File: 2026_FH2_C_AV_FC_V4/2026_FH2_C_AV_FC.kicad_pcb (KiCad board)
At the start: 4 copper layers, 80 x 80 mm, 258 parts, among them IC1 BMP390, IC2 BMP390, IC3 BMP390, IC4 BMP390, IC5 TPS22919DCKR, IC6 TPS22919DCKR, IC7 TPS22919DCKR, IC8 ADXL375BCCZ, IC9 CD4051BPWR, J1 CON-SMA-EDGE-S, J10 MUSB-05-S-B-SM-A-K-TR, J11 DIN41612_02x16_AB, J2 Screw_Terminal_01x02, J3 Screw_Terminal_01x02, J4 Screw_Terminal_01x02, J5 Screw_Terminal_01x02, J6 Micro_SD_Card_Det_Hirose_DM3AT, J7 Conn_01x04_Pin, J8 Conn_01x04_Pin, J9 MUSB-05-S-B-SM-A-K-TR, Q1 IRLML2502, Q2 IRLML6344TRPBF, Q3 IRLML6344TRPBF, Q4 IRLML6344TRPBF, Q5 IRLML6344TRPBF, Q6 IRLML6344TRPBF, Q7 IRLML6344TRPBF, SW1 SW_SPDT, SW2 SW_Push_SPDT, U1 MCP1727-3302xSN, U10 ICM-45605, U11 ICM-45605, U12 MAX3226, U13 SPINE_LT3960, U14 MCP2542FDxMF, U15 MCP2542FDxMF, U16 TMP1075DSG, U2 TPS2116DRL, U3 STM32H743ZITx, U4 RGBLED_1, U5 RGBLED_2, U6 RGBLED_3, U7 MAX-M10S, U8 ICM-45605, U9 ICM-45605, Y1 26Mhz

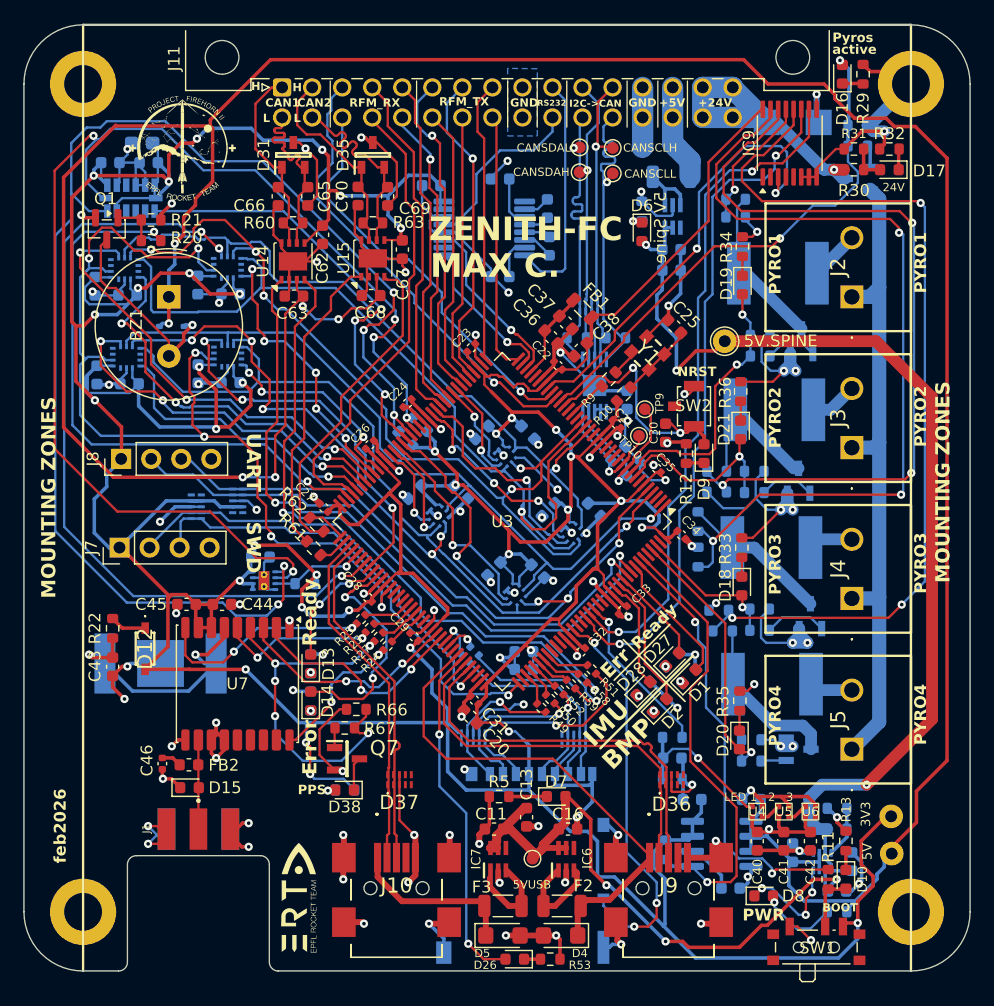
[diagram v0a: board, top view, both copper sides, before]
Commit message: FC FIX: DIN41612 was not centered
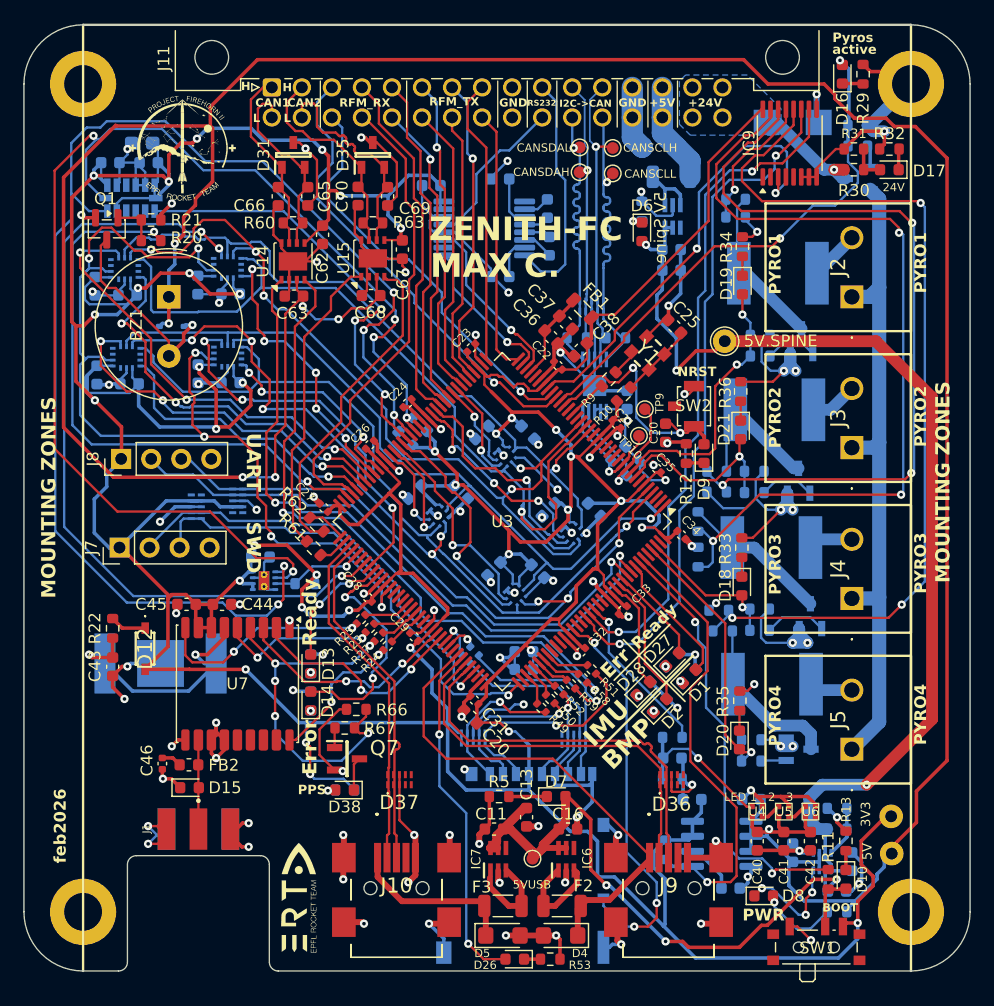
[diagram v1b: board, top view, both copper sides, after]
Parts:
- moved J11 0.87 mm to (140.0, 51.3)
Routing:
- net +24V: track 24.3 -> 9.47 mm
- net /Project Architecture/CAN RS232 and other connections/TX_RS232: track 15.0 -> 13.5 mm
- net /Project Architecture/CAN RS232 and other connections/CAN2_L: track 17.6 -> 18.9 mm
- net /Project Architecture/CAN RS232 and other connections/CANSCLL: track 27.1 -> 26.0 mm
- net /Project Architecture/SPINE/SPI_RFM_TX_MOSI: track 28.0 -> 27.0 mm
- net /Project Architecture/CAN RS232 and other connections/CAN2_H: track 17.6 -> 18.3 mm
- net /Project Architecture/SPINE/SPI_RFM_TX_CS: track 26.5 -> 25.8 mm
- net +5V: track 269.4 -> 270.0 mm
- net /Project Architecture/CAN RS232 and other connections/CANSDAH: track 25.1 -> 24.4 mm
- net /Project Architecture/SPINE/GPIO_RFM_TX_INT0: track 23.8 -> 24.4 mm
- net /Project Architecture/CAN RS232 and other connections/CAN1_H: track 16.8 -> 16.3 mm
- added copper zone on B.Cu, net +24V
- removed copper zone on B.Cu, net GND
